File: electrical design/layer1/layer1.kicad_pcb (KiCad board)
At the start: 2 copper layers, 178 x 158.1 mm, 115 parts, among them J1 Conn_01x06_Female, J2 Conn_01x04_Male, J3 Conn_01x04_Male, J4 Conn_01x03_Female, J5 Conn_01x02_Female, Q1 MOSFET-NCH-FQP30N06L, Q2 MOSFET-NCH-AO3404A, Q3 MOSFET-NCH-FQP30N06L, Q4 MOSFET-NCH-AO3404A, SW3 SW_Push, U1 STM32F103C8T6, U2 CD74HC4067SM, U3 CD74HC4067SM

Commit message: update layer 1 and layer 3 pcbs
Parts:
- removed C12: 1500pF, Capacitor_SMD:C_0603_1608Metric
- removed D36: 1N4728, Diode_THT:D_DO-41_SOD81_P10.16mm_Horizontal
- removed D37: 1N5401, Diode_THT:D_DO-27_P15.24mm_Horizontal
- removed J2, J3: Conn_01x04_Male, Connector_PinHeader_2.54mm:PinHeader_1x04_P2.54mm_Vertical
- removed Q3: MOSFET-NCH-FQP30N06L, Package_TO_SOT_THT:TO-220-3_Vertical
- removed Q4: MOSFET-NCH-AO3404A, Package_TO_SOT_SMD:TSOT-23
- removed R46, R48: 10k, Resistor_SMD:R_0603_1608Metric
- removed R47: 1k, Resistor_SMD:R_0603_1608Metric
- removed R49: 20, Resistor_SMD:R_0603_1608Metric
- removed SOLENOID2: Conn_01x02_Female, Connector_AMASS:AMASS_XT30UPB-F_1x02_P5.0mm_Vertical
- added SW1: SW_DPDT_x2, Switches:SWITCH_SPDT_PTH_11.6X4.0MM_LOCK, F.Cu at (110.0, 176.7)
- added SW2: SW_DPDT_x2, Switches:SWITCH_SPDT_PTH_11.6X4.0MM_LOCK, F.Cu at (110.0, 183.9)
- added Y1: Crystal, Crystal:Crystal_SMD_5032-2Pin_5.0x3.2mm, F.Cu at (94.8, 103.8)
- C1, R33: moved to B.Cu
- J1: value Conn_01x06_Female -> SH1.0 Female
- J4: value Conn_01x03_Female -> TEST
- moved J4 115.8 mm to (94.2, 177.7), turned to 0 degrees
- moved C1 110.3 mm to (110.0, 170.9), turned to -90 degrees
- moved SW3 92.0 mm to (119.2, 180.4)
- moved J1 91.0 mm to (126.8, 180.5)
- moved R33 90.0 mm to (105.8, 171.0), turned to 90 degrees
- moved R39 67.3 mm to (107.8, 191.0), turned to -90 degrees
- moved D33 66.9 mm to (112.2, 191.0), turned to -90 degrees
- moved R40 56.7 mm to (120.0, 185.5), turned to 180 degrees
- moved R41 55.5 mm to (119.2, 175.8), turned to 90 degrees
- moved R38 31.8 mm to (110.5, 101.0)
- moved C8 11.2 mm to (89.0, 101.7), turned to -90 degrees
- moved C10 7.75 mm to (36.7, 117.8)
- moved C11 7.75 mm to (47.9, 94.6)
- moved D34 7.75 mm to (44.5, 106.3)
- moved D35 7.75 mm to (41.4, 106.3)
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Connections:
- net /SOLENOID1ON renamed /SOLENOIDON
- U1 pad 29: /SOLENOID2ON -> unconnected-(U1-Pad29)
- U1 pad 38: /M4EB -> unconnected-(U1-Pad38)
- U1 pad 39: /M4EA -> unconnected-(U1-Pad39)
- U1 pad 40: /M2EB -> unconnected-(U1-Pad40)
- U1 pad 41: /M2EA -> unconnected-(U1-Pad41)
- U1 pad 42: /M1EA -> unconnected-(U1-Pad42)
- U1 pad 43: /M1EB -> unconnected-(U1-Pad43)
- U1 pad 45: /M3EA -> unconnected-(U1-Pad45)
- U1 pad 46: /M3EB -> unconnected-(U1-Pad46)
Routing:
- net Net-(R16-Pad2): track 87.2 -> 0.00 mm
- net Net-(R17-Pad2): track 60.3 -> 0.00 mm
- net Net-(D37-Pad2): track 38.6 -> 0.00 mm
- net /M3EB: track 35.3 -> 0.00 mm
- net /M1EB: track 35.3 -> 0.00 mm
- net /M1EA: track 35.2 -> 0.00 mm
- net /M3EA: track 34.8 -> 0.00 mm
- net /S1: track 57.0 -> 84.0 mm
- net /M4EB: track 23.0 -> 0.00 mm
- net /M4EA: track 22.9 -> 0.00 mm
- net /S0: track 65.1 -> 88.0 mm
- net /M2EB: track 22.8 -> 0.00 mm
- net /M2EA: track 22.7 -> 0.00 mm
- net /SOLENOIDPOWER: track 42.9 -> 22.5 mm
- net /OSCIN: track 0.00 -> 20.2 mm, vias 0 -> 2
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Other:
- outline, holes or cut-outs redrawn
- board text removed: "BACK"

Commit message: almost final pcbs
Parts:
- added J2: SH1.0 5P, Connector_JST:JST_SH_BM05B-SRSS-TB_1x05-1MP_P1.00mm_Vertical, F.Cu at (140.8, 112.5)
- J4: value TEST -> Conn_01x03_Female
- moved SW2 112.7 mm to (177.0, 93.4), turned to 90 degrees
- moved R39 107.9 mm to (183.0, 113.6)
- moved J1 106.0 mm to (188.0, 94.0), turned to 0 degrees
- moved D33 101.9 mm to (183.0, 117.6), turned to 90 degrees
- moved C9 89.8 mm to (176.0, 128.0)
- moved C8 87.1 mm to (172.0, 128.0), turned to 90 degrees
- moved R40 84.9 mm to (183.0, 128.6), turned to 90 degrees
- moved SW3 83.9 mm to (181.0, 123.6), turned to 180 degrees
- moved R41 82.7 mm to (179.0, 118.6)
- moved Y1 81.7 mm to (174.0, 123.6), turned to 180 degrees
- moved FB1 75.5 mm to (175.7, 119.4), turned to 90 degrees
- moved C7 75.3 mm to (177.0, 101.6)
- moved C6 74.4 mm to (175.0, 101.6)
- moved C5 70.8 mm to (173.0, 101.6)
- moved FB2 70.2 mm to (177.0, 98.0)
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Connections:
- U1 pad 12: unconnected-(U1-Pad12) -> /DEBUGTX
- U1 pad 14: /DEBUGTX -> unconnected-(U1-Pad14)
- U1 pad 2: /BATT_LVL -> unconnected-(U1-Pad2)
- U1 pad 47: GNDA -> GND
- U1 pad 8: GND -> GNDA
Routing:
- net /SOLENOIDON: track 11.9 -> 210.3 mm, vias 0 -> 2
- net /S3: track 34.7 -> 179.2 mm, vias 3 -> 6
- net /S2: track 31.5 -> 170.7 mm, vias 1 -> 5
- net /S1: track 84.0 -> 199.6 mm, vias 3 -> 7
- net /S0: track 88.0 -> 198.5 mm, vias 3 -> 7
- net /MCU3V3: track 37.3 -> 85.4 mm, vias 0 -> 1
- net /MUX2OUT: track 27.4 -> 73.1 mm, vias 1 -> 3
- net /MUX1OUT: track 47.2 -> 85.8 mm, vias 1 -> 3
- net /DEBUGTX: track 0.00 -> 28.9 mm, vias 0 -> 2
- net /DEBUGRX: track 0.00 -> 27.8 mm, vias 0 -> 2
- net /SWDCLOCK: track 0.00 -> 24.4 mm, vias 0 -> 2
- net GNDA: track 3.21 -> 26.2 mm, vias 0 -> 2
- net /SWDIO: track 0.00 -> 22.2 mm
- net GND: track 12.4 -> 25.9 mm
- net /PROG3V3: track 0.00 -> 11.5 mm
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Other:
- outline, holes or cut-outs redrawn

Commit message: production-ready layer 1!
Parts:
- removed R33: 0.39, Resistor_SMD:R_0603_1608Metric
- added J5: Conn_01x02_Male, Connector_PinHeader_2.54mm:PinHeader_1x02_P2.54mm_Vertical, F.Cu at (75.0, 37.7)
- added J6: Conn_01x02_Male, Connector_PinHeader_2.54mm:PinHeader_1x02_P2.54mm_Vertical, F.Cu at (145.0, 37.7)
- J3: renamed from J4; value Conn_01x03_Female -> DEBUG
- moved SW1 113.9 mm to (35.0, 91.0)
- moved J3 108.5 mm to (27.0, 92.5)
- moved C1 101.2 mm to (52.0, 88.0), turned to 180 degrees
- moved R1 2.00 mm to (104.1, 50.3)
- moved R32 2.00 mm to (115.9, 50.3)
- moved D1 1.50 mm to (110.0, 49.5)
- moved D2 1.00 mm to (98.1, 50.2)
- moved D32 1.00 mm to (121.9, 50.2)
- renumbered J5 to J4
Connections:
- SW1 pad 2: Net-(R33-Pad1) -> Net-(C1-Pad1)
- U1 pad 14: unconnected-(U1-Pad14) -> /LIGHTGATE
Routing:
- net +5V: track 0.00 -> 210.9 mm
- net +3V3: track 4.67 -> 206.1 mm, vias 0 -> 3
- net GND: track 25.9 -> 133.6 mm, vias 36 -> 63
- net /LIGHTGATE: track 0.00 -> 94.9 mm, vias 0 -> 2
- net Net-(R16-Pad2): track 0.00 -> 70.2 mm
- net /TX: track 2.06 -> 59.3 mm, vias 1 -> 4
- net /RX: track 2.06 -> 57.9 mm, vias 1 -> 4
- net Net-(R17-Pad2): track 0.00 -> 38.2 mm
- net VCCQ: track 381.2 -> 416.6 mm
- net Net-(R1-Pad2): track 59.8 -> 54.8 mm
- net Net-(C1-Pad1): track 4.25 -> 8.41 mm, vias 0 -> 2
- net Net-(R32-Pad2): track 86.5 -> 82.9 mm
- net GNDA: track 26.2 -> 23.8 mm
- net /S2: track 170.7 -> 169.7 mm
- net /SWDCLOCK: track 24.4 -> 25.3 mm
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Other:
- board size 178 x 158.1 mm -> 178 x 167.5 mm
- board text removed: "+3V3"
- board text removed: "+5V"
- board text removed: "BOOST"
- board text removed: "FRONT"
- board text removed: "GND"

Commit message: submit all pcbs for production
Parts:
- added R33: 4.7k, Resistor_SMD:R_0603_1608Metric, B.Cu at (145.8, 45.8)
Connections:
- C2 pad 2: GND -> GNDA
- C3 pad 2: GND -> GNDA
- R34 pad 2: GND -> GNDA
- R35 pad 2: GND -> GNDA
- R36 pad 2: GND -> GNDA
- R37 pad 2: GND -> GNDA
- U2 pad 12: GND -> GNDA
- U3 pad 12: GND -> GNDA
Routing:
- net GNDA: track 23.8 -> 281.9 mm, vias 2 -> 12
- net GND: track 133.6 -> 68.3 mm, vias 63 -> 58
- net /LIGHTGATE: track 94.9 -> 100.4 mm
- net Net-(R1-Pad2): track 54.8 -> 55.3 mm
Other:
- outline, holes or cut-outs redrawn

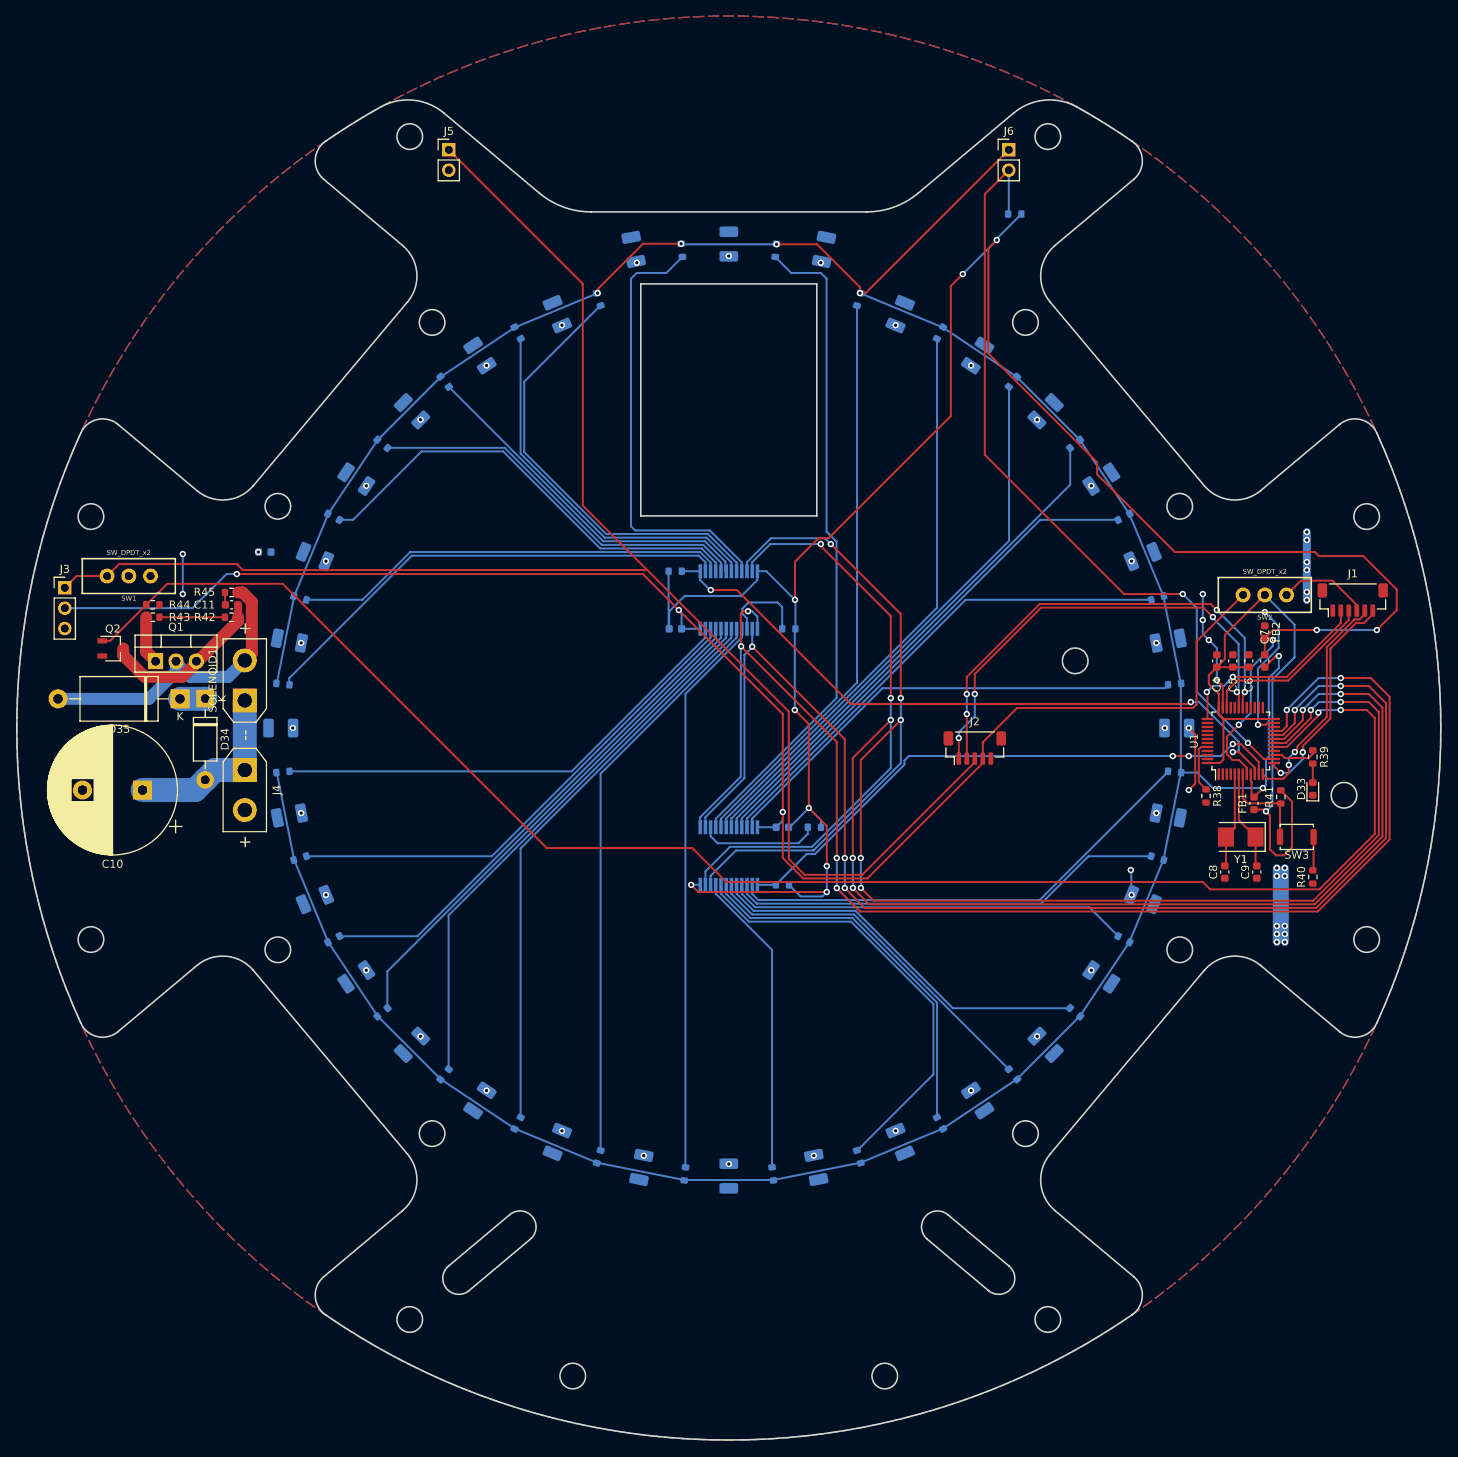
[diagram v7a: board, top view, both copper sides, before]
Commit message: fillet pcb traces
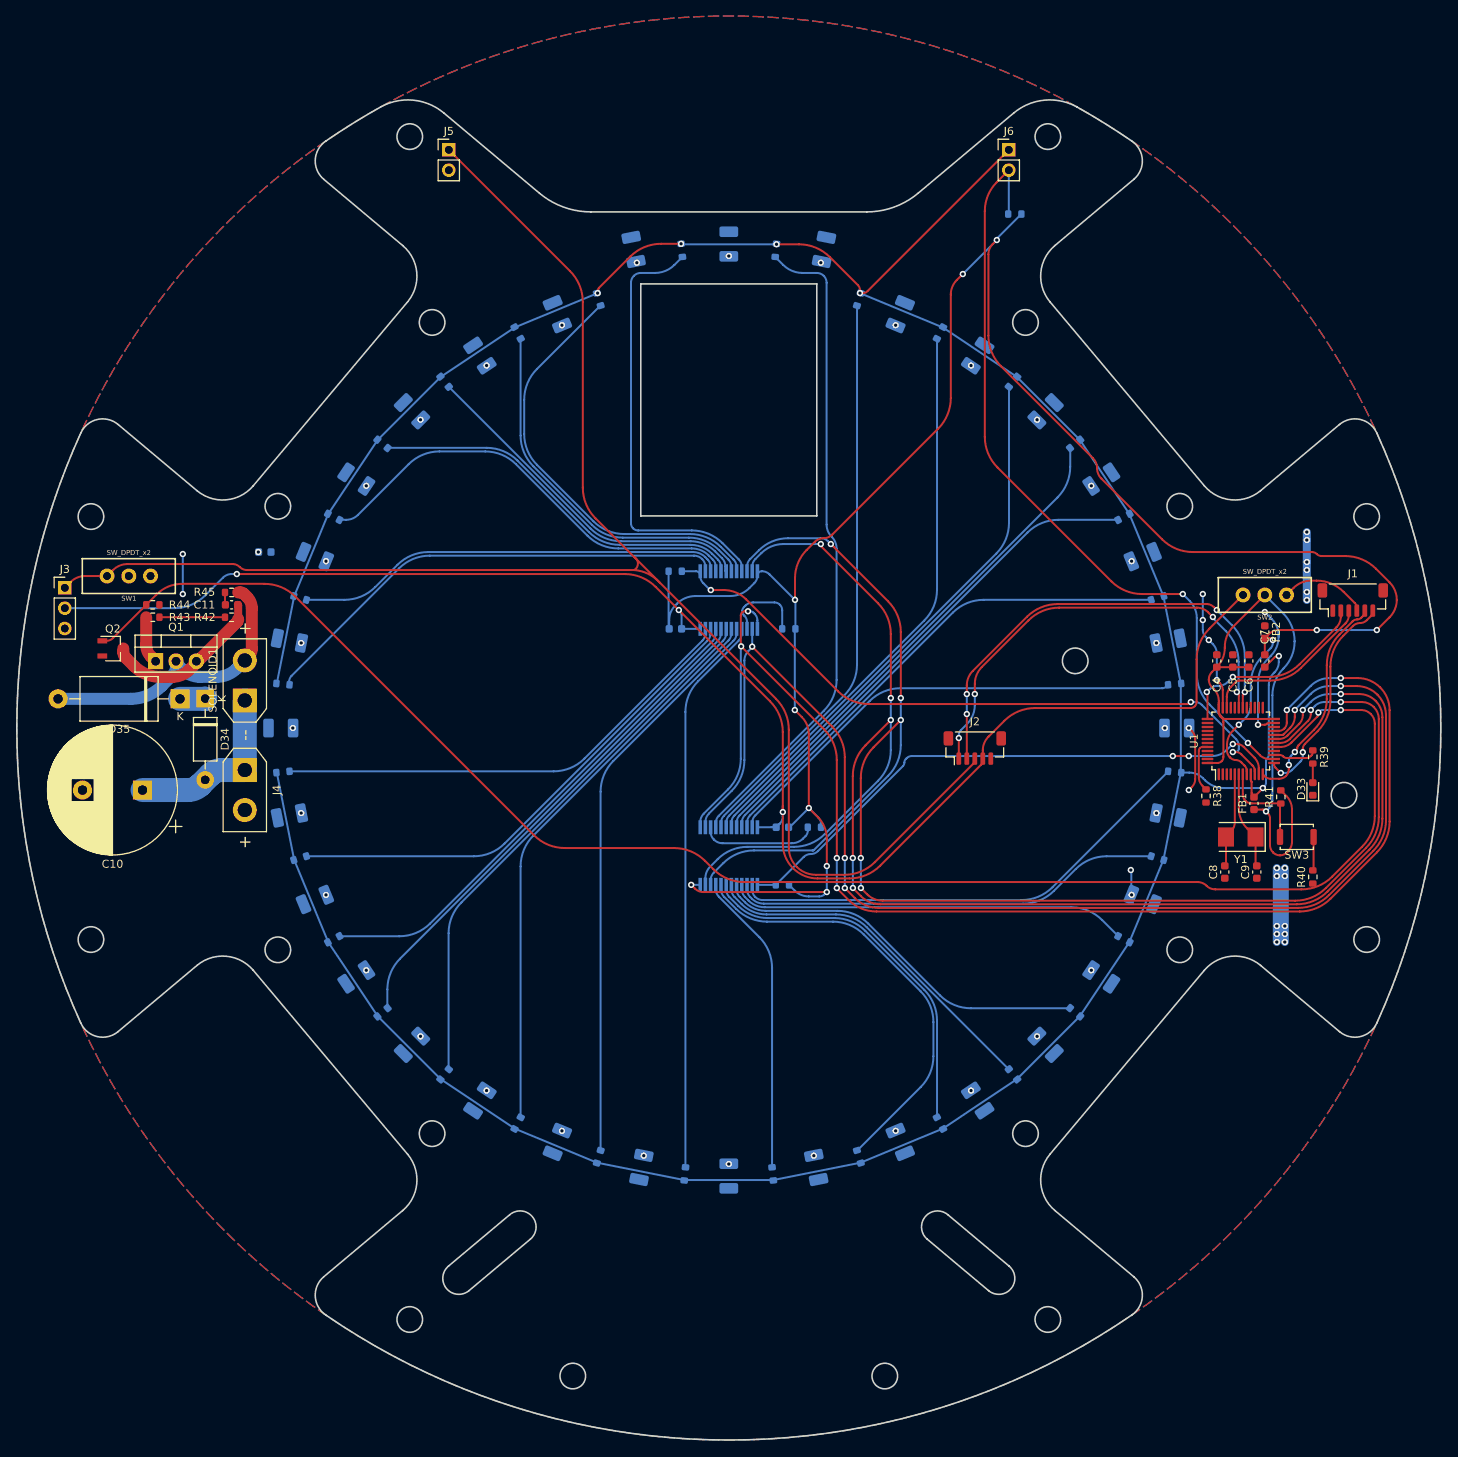
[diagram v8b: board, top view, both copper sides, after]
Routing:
- net GNDA: track 281.9 -> 277.4 mm
- net /S1: track 199.4 -> 196.5 mm
- net /S0: track 198.4 -> 195.9 mm
- net /SOLENOIDON: track 210.3 -> 208.0 mm
- net +3V3: track 206.1 -> 203.9 mm
- net /S3: track 179.2 -> 177.1 mm
- net +5V: track 210.9 -> 213.0 mm
- net /S2: track 169.7 -> 167.7 mm
- net /MCU3V3: track 86.2 -> 84.6 mm
- net VCCQ: track 416.6 -> 415.2 mm
- net /LIGHTGATE: track 100.4 -> 99.1 mm
- net Net-(R18-Pad2): track 55.7 -> 54.6 mm
- net Net-(R2-Pad2): track 55.6 -> 54.5 mm
- net Net-(R6-Pad2): track 57.4 -> 56.4 mm
- net Net-(D35-Pad2): track 37.7 -> 36.7 mm
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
